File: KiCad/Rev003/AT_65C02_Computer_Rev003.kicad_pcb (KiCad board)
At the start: 2 copper layers, 241.3 x 149.9 mm, 164 parts, among them J1 CLK Jumper, J11 LCD Connector, J12 System Bus Output port, J14 ESP Interface, J15 Level_Shifter_HV, J16 Level_Shifter_LV, J18 CPU Signals, J2 Optional UART Port, J20 Modem Interface, J21 Expansion port #2, J22 Expansion port #3, J27 LED SWITCH, J29 Decoder Signals, J3 Conn_01x06_Female, J30 Standard Decoder Jumpers, J31 Memory Decoder Expansion, J32 Decoder Expansion, J33 VIA2PA, J4 AudioJack4, J5 Barrel_Jack-Connector, J6 Mini-DIN-6, J7 Expansion port, J8 AVR-ISP-10, J9 VIA2PB, Q1 BC547, SW1 SW_SPDT, SW2 Step, SW3 Mode, SW4 SW_SPDT, U1 74HC21, U10 ATtiny4313-PU, U11 65C22S, U12 65C22S, U13 LM3940, U14 74LS04, U15 74LS08, U16 74LS32, U17 NE555, U18 NE555, U19 NE555, U2 74HC00, U20 74HCT540, U21 74HCT573, U22 74HCT573, U23 74HCT573, U24 10_LED_Array (yellow), U25 10_LED_Array (green), U26 10_LED_Array (red), U27 10_LED_Array (red), U28 LM393, U3 74HC02, U4 NE555, U5 65C51N, U6 Regulator_Linear_L7805, U7 65C02S, U8 28C256, U9 62256, X1 1MHz, X2 1.8432MHz

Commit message: Pads changed
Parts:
- U20, U21, U22, U23: footprint Package_DIP:DIP-20_W7.62mm_Socket_LongPads -> Package_DIP:DIP-20_W7.62mm_Socket
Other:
- board text added: "3.3"
- board text added: "Tx"

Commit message: Silkscreen updates
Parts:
- moved C21 119.4 mm to (308.4, 156.2)
- moved C25 119.4 mm to (274.0, 89.2)
- moved D8 119.4 mm to (290.0, 185.6)
- moved R11 119.4 mm to (293.6, 128.2)
- moved R21 119.4 mm to (291.0, 170.8)
- moved U15 119.4 mm to (308.4, 163.5)
- moved U17 119.4 mm to (282.8, 142.9)
- moved U18 119.4 mm to (308.4, 142.9)
- moved C12 119.4 mm to (180.0, 127.5)
- moved C13 119.4 mm to (181.9, 133.7)
- moved C14 119.4 mm to (197.3, 133.7)
- moved C17 119.4 mm to (257.9, 78.6)
- moved C18 119.4 mm to (283.1, 137.3)
- moved C2 119.4 mm to (251.0, 102.8)
- moved C22 119.4 mm to (283.1, 129.5)
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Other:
- board text added: "BE"
- board text added: "~SO"

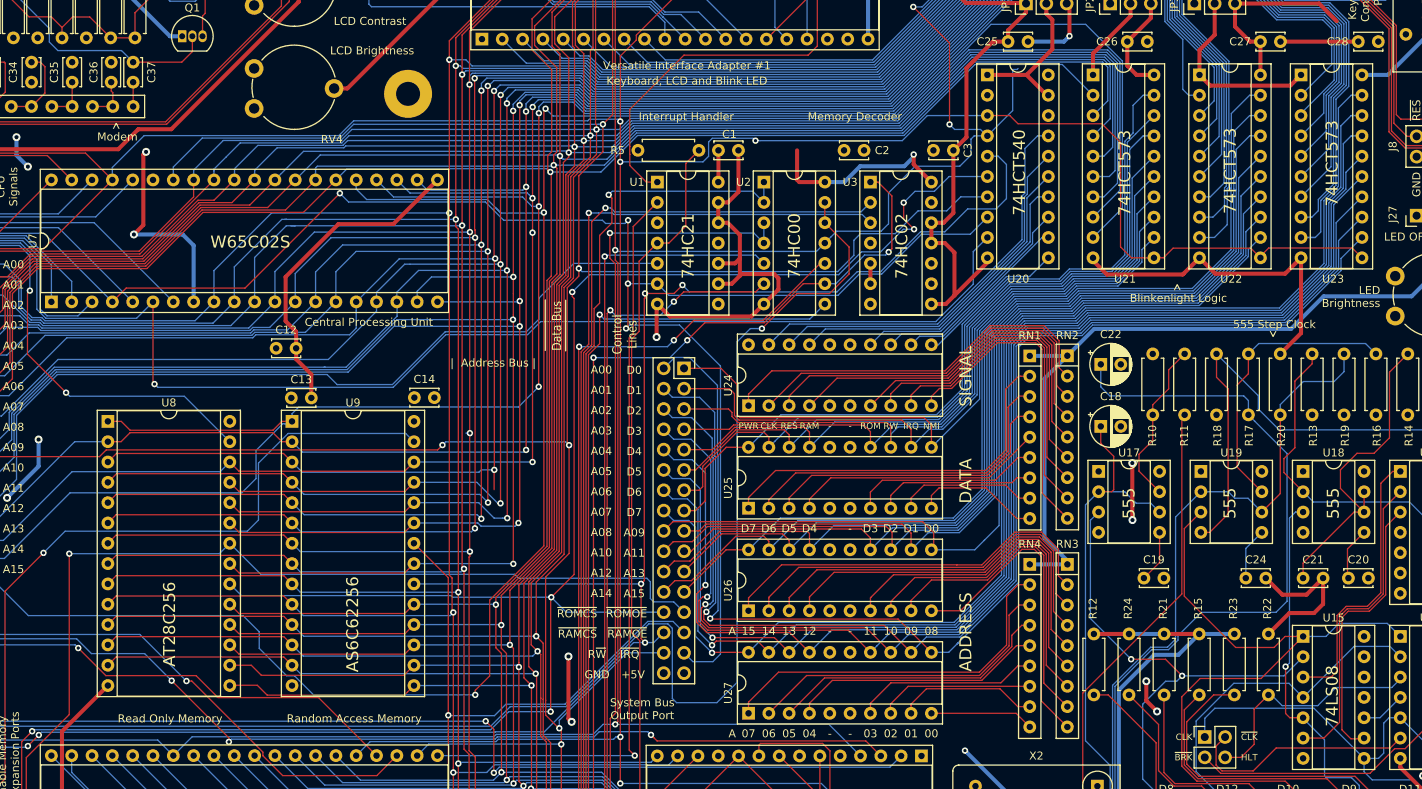
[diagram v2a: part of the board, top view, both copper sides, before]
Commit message: U8 ZIF socket
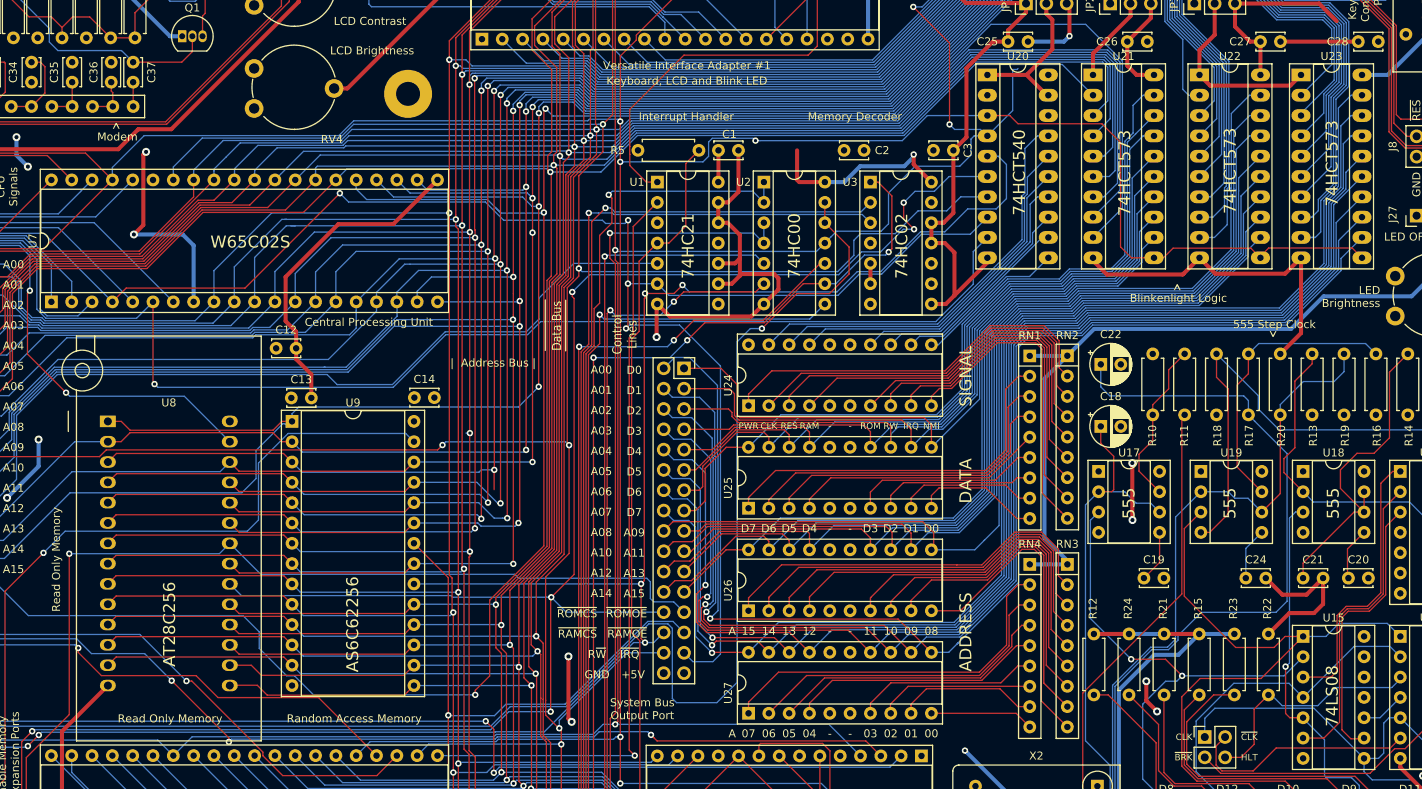
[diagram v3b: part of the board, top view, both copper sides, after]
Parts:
- U20, U21, U22, U23: footprint Package_DIP:DIP-20_W7.62mm_Socket -> Package_DIP:DIP-20_W7.62mm_Socket_LongPads
- U8: footprint Package_DIP:DIP-28_W15.24mm_Socket -> Socket:DIP_Socket-28_W11.9_W12.7_W15.24_W17.78_W18.5_3M_228-1277-00-0602J
